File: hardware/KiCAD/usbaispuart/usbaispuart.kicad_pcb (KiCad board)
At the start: 2 copper layers, 81.5 x 41.7 mm, 52 parts, among them J1 AVR-ISP-UART-PROGRAMER-10, J2 LED Connector, J3 LED Connector, J4 USB_B, J5 Reset Jumper, J6 5V / 3.3 Selection Jumper, J7 Power Out Jumper, Q1 2N2222A, Q2 2N2222A, U1 SN74AHC367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

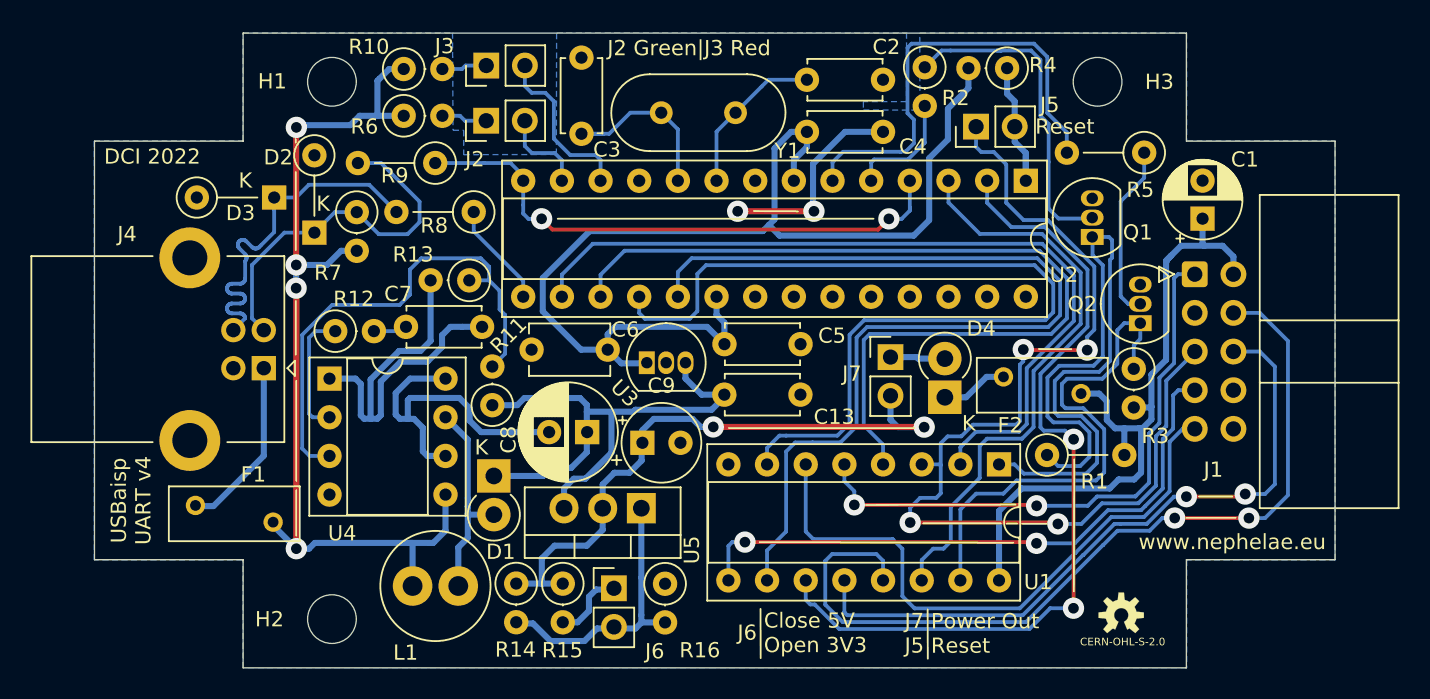
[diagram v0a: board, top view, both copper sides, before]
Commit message: Fixed an error on 2N2222A symbol.
+ Added 2N2222A datasheet.
+ Regenerate PCB images.
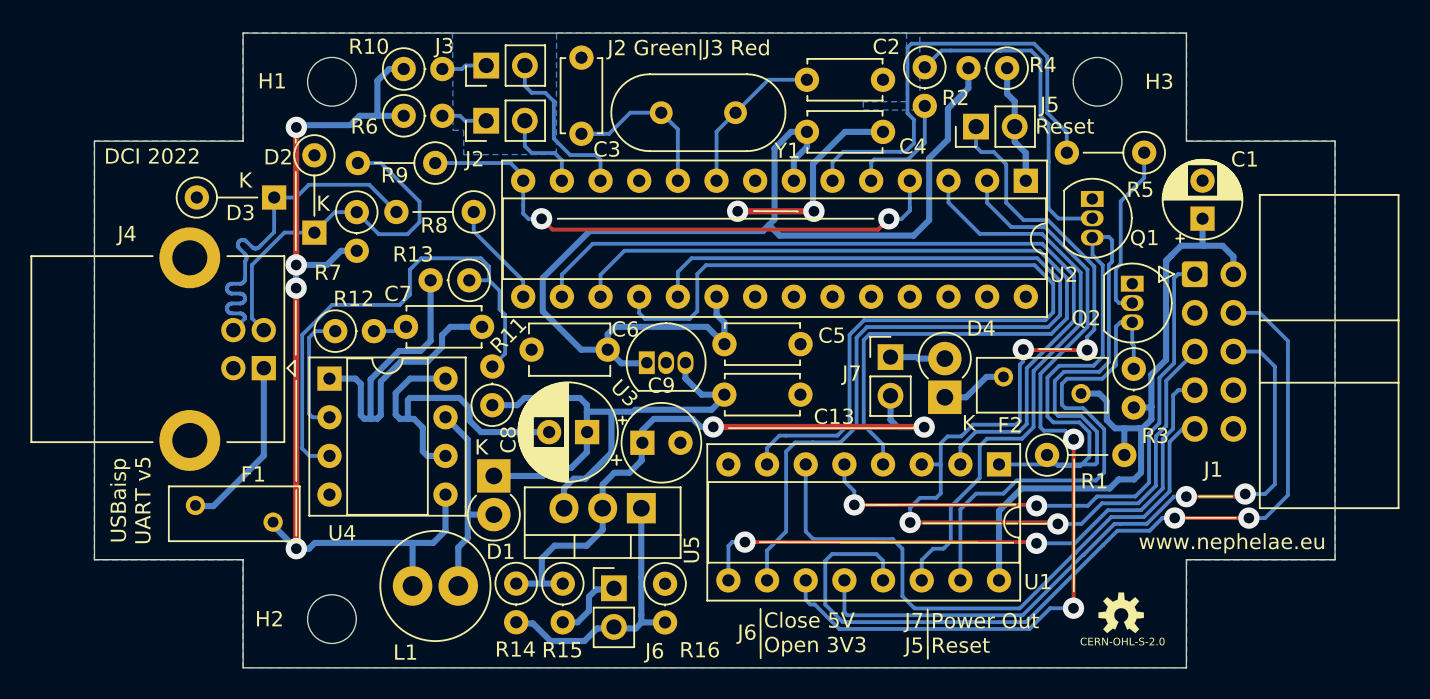
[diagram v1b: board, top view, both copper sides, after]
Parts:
- F2: value Polyfuse 250 mA -> Polyfuse 200 / 250 mA
- moved Q2 2.65 mm to (174.6, 89.3), turned to 270 degrees
- moved Q1 2.50 mm to (172.0, 83.8), turned to 270 degrees
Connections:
- Q1 pad 1: SPI_BUFFER_EN -> GND
- Q1 pad 3: GND -> SPI_BUFFER_EN
- Q2 pad 1: UART_BUFFER_EN -> GND
- Q2 pad 3: GND -> UART_BUFFER_EN
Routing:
- net SPI_BUFFER_EN: track 50.9 -> 50.4 mm
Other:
- board text added: "USBaisp UART v5"
- board text removed: "USBaisp UART v4"

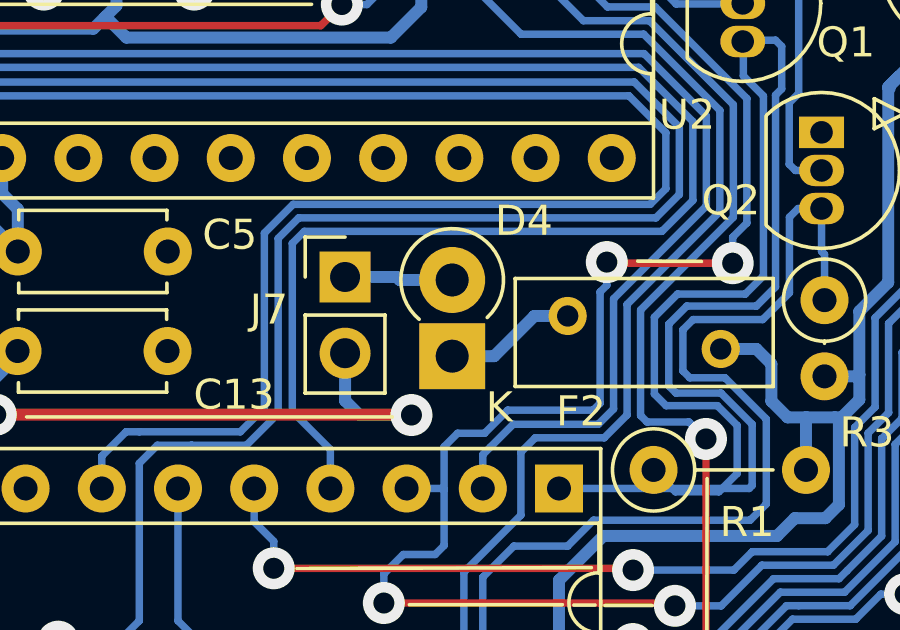
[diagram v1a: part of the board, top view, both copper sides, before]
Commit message: Change D4 from 1N5819 to the correct 1N5817
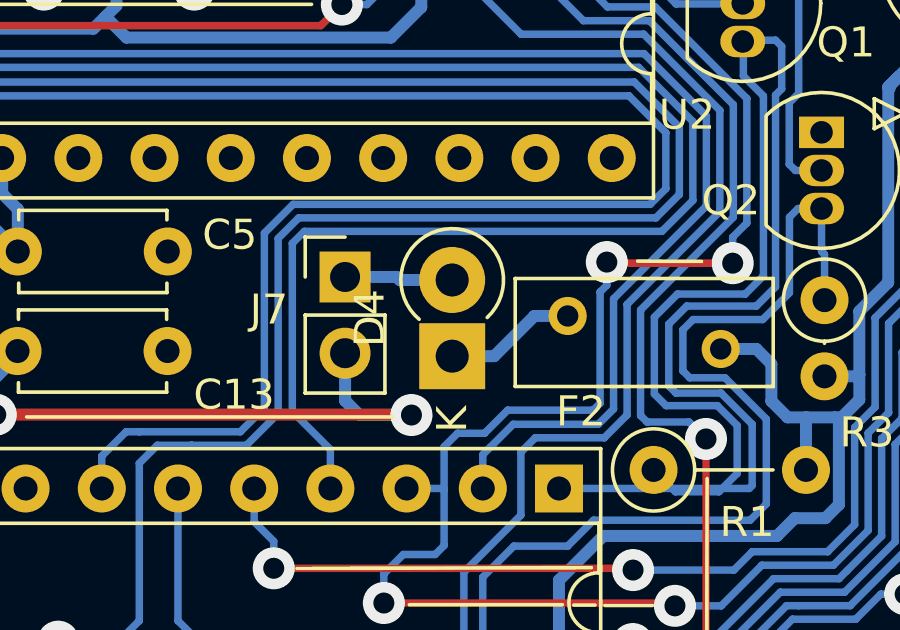
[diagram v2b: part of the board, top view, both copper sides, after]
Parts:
- D4: value 1N5819 -> 1N5817
